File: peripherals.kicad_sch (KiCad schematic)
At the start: 61 parts, among them J801 Socket_Samtec_ERF5_2x20_ERF5-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, J802 JST_SH_1x4_SM04B-SRSS-TB-LF-SN, J803 JST_SH_1x4_SM04B-SRSS-TB-LF-SN, J804 JST_SH_1x2_SM02B-SRSS-TB-LF-SN, J805 JST_SH_1x6_SM06B-SRSS-TB-LF-SN, U801 PN7160A1_VFQFN, Y801 Resonator_27.12MHz_XRCGB

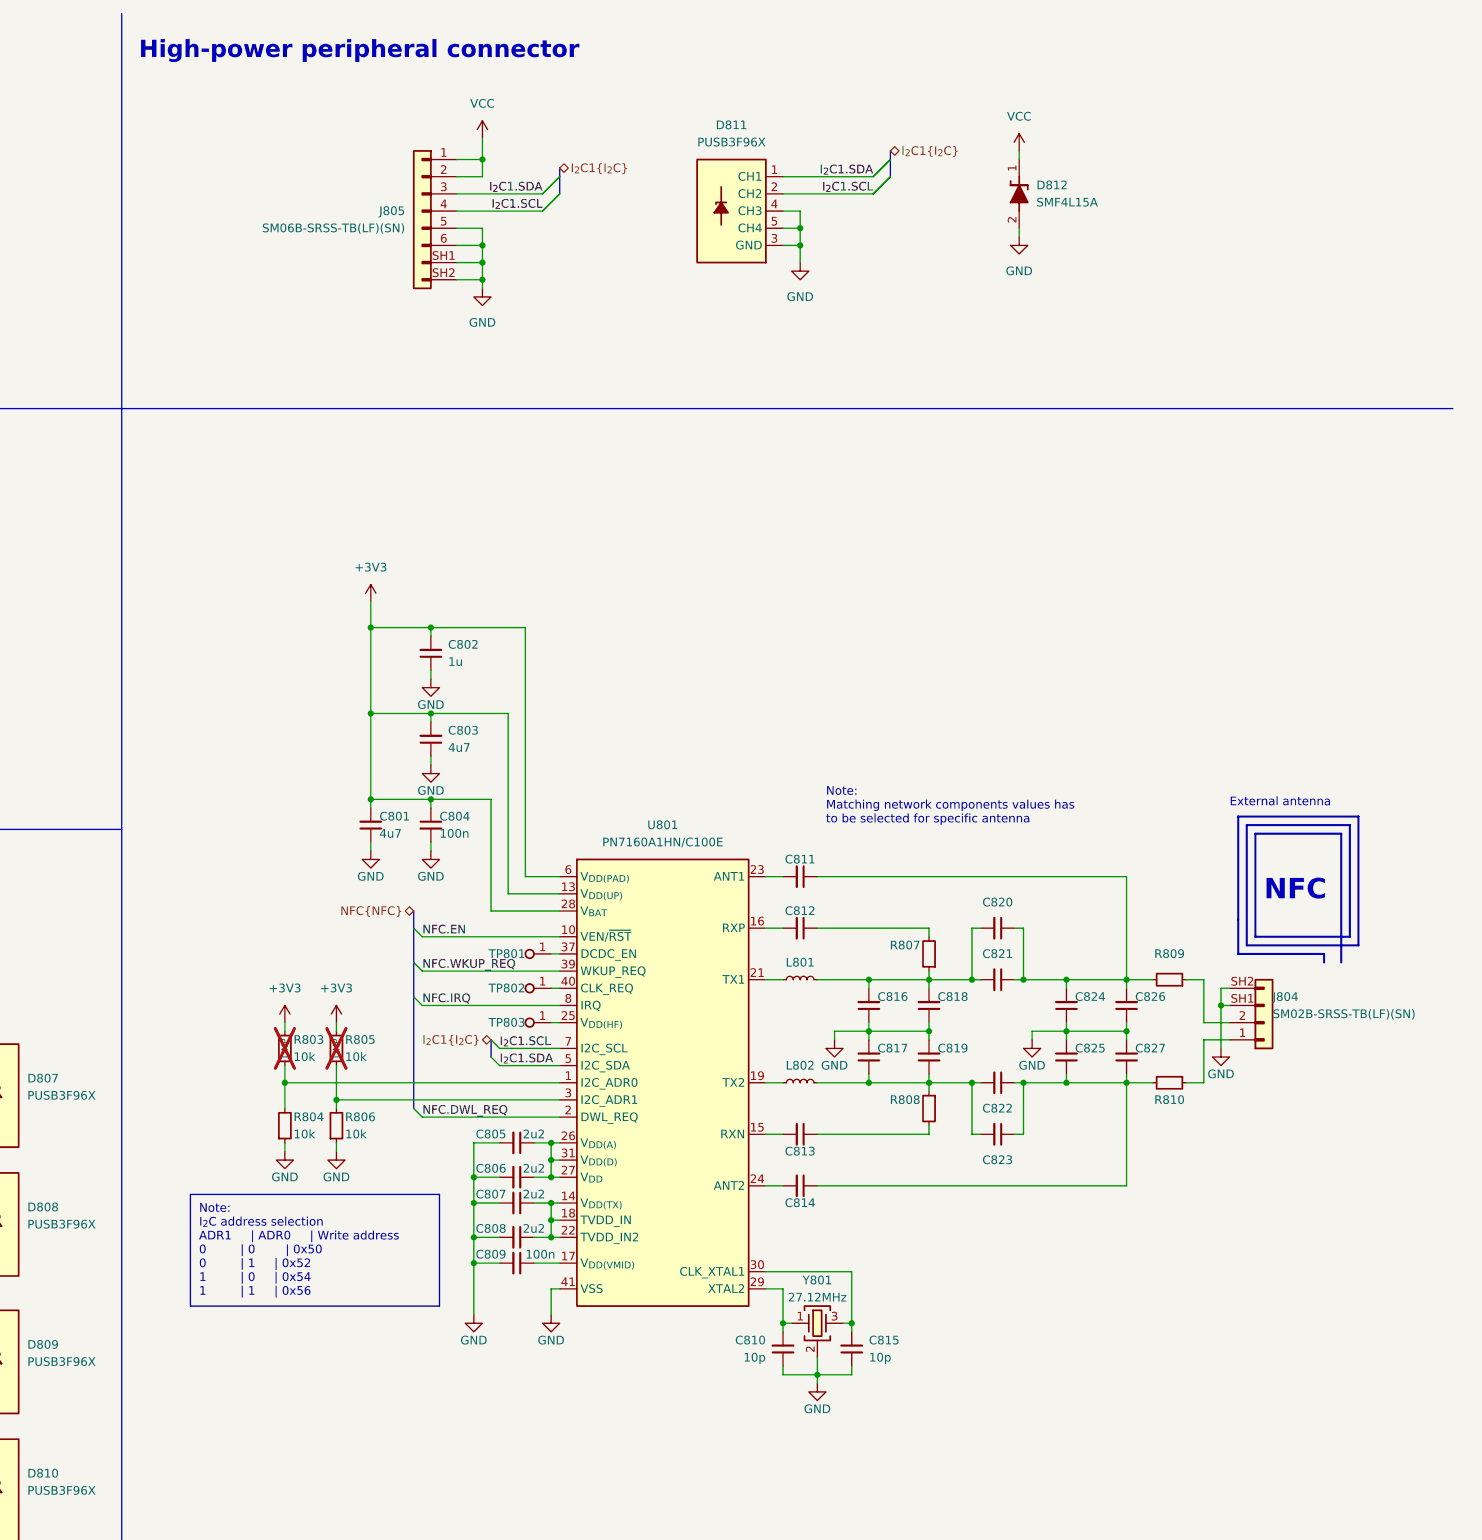
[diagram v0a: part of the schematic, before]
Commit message: Revert "[#58133] Add high-power peripheral connector"
This reverts commit a83347aca41b3b449620dbb955cb5f6a2460727a
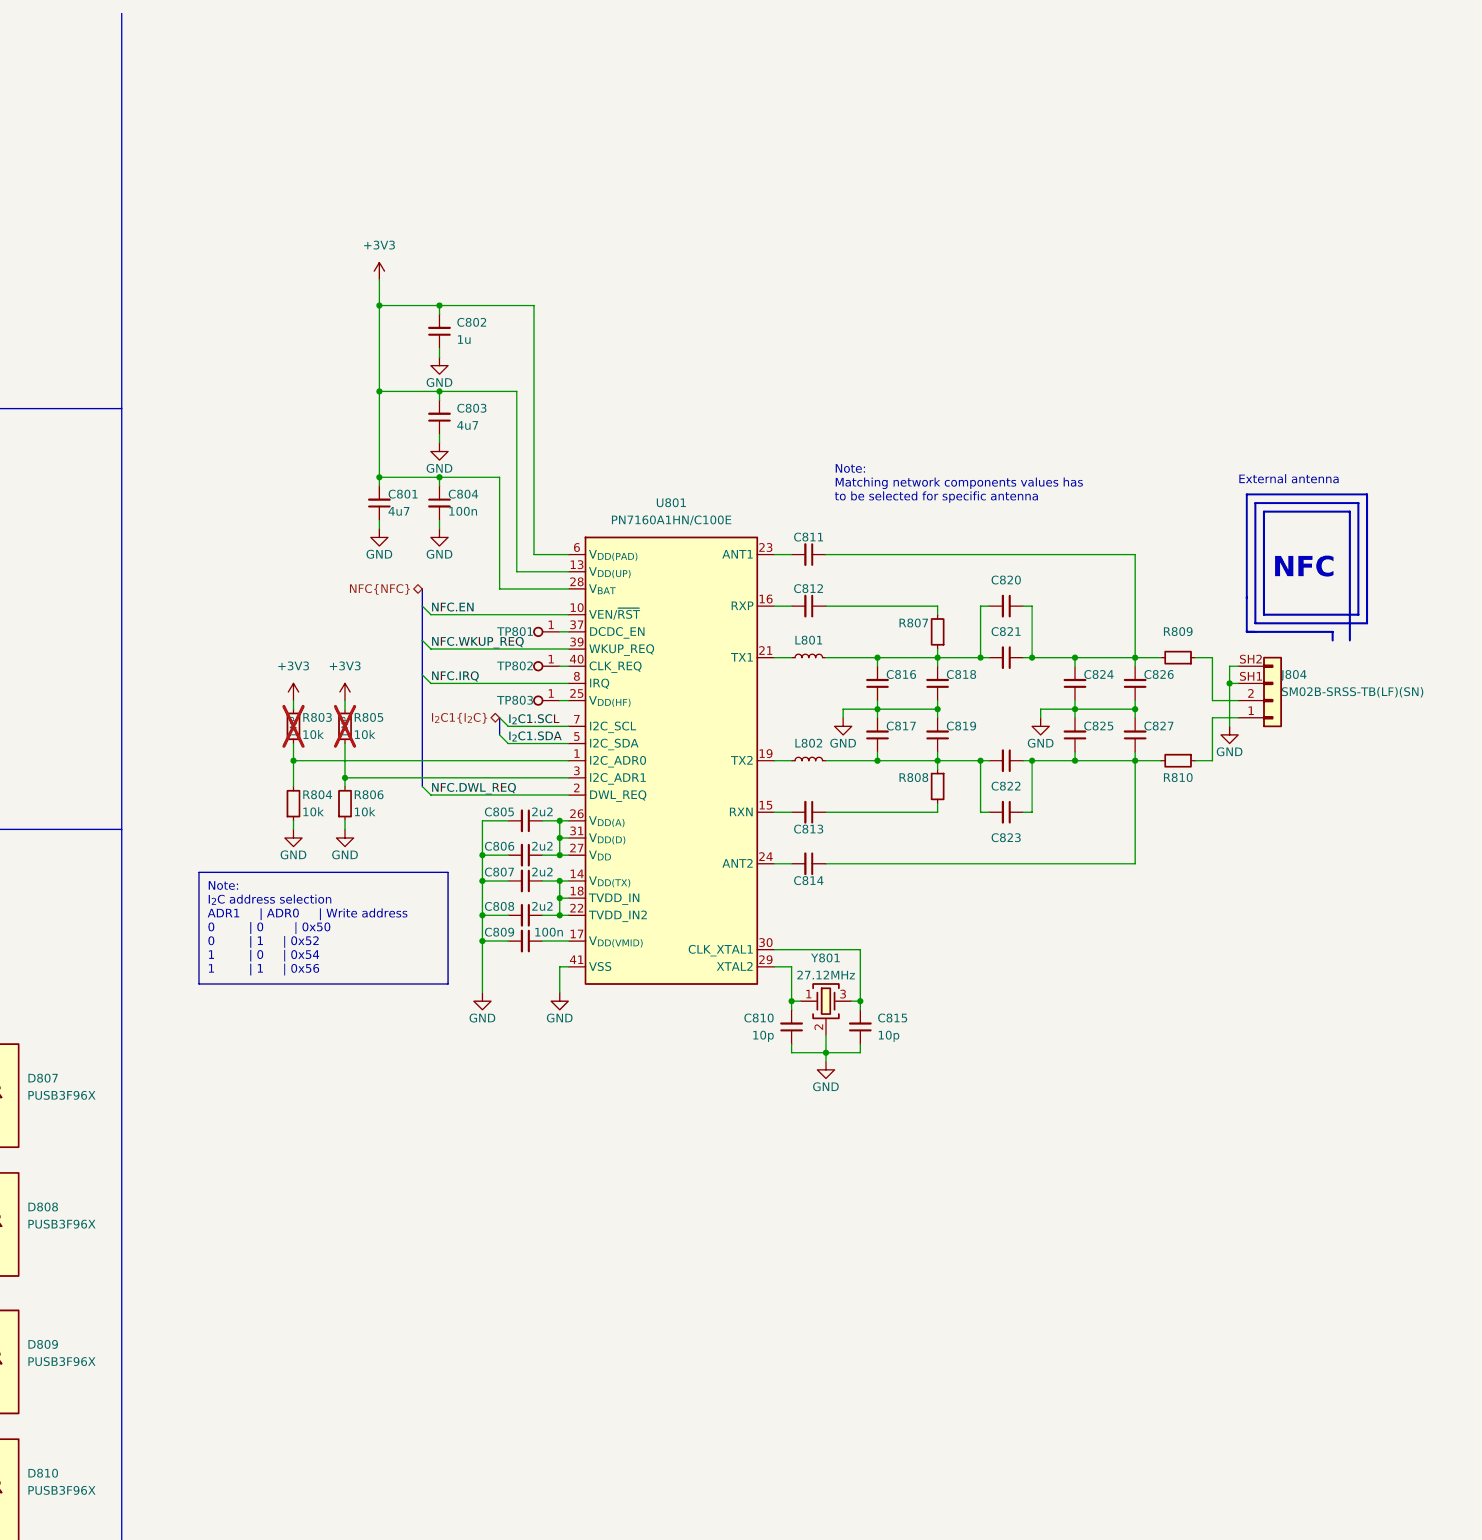
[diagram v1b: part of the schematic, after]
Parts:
- removed D811: PUSB3F96X_PASS, antmicro-footprints:Nexperia_DFN-10_2.5x1mm_P0.5mm, symbol antmicroTVSDiodes:PUSB3F96X_PASS
- removed D812: SMF4L15A, antmicro-footprints:SOD-123FL, symbol antmicroTVSDiodes:SMF4L15A
- removed J805: JST_SH_1x6_SM06B-SRSS-TB-LF-SN, antmicro-footprints:Conn_JST_SH_1x6_SM06B-SRSS-TB-LF-SN, symbol antmicroWire2BoardConnectors:JST_SH_1x6_SM06B-SRSS-TB-LF-SN
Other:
- note removed: "High-power peripheral connector"
- moved on the sheet: C801, C802, C803, C804, C805, C806, C807, C808, C809, C810, C811, C812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

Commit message: [#58133] Add high-power peripheral connector
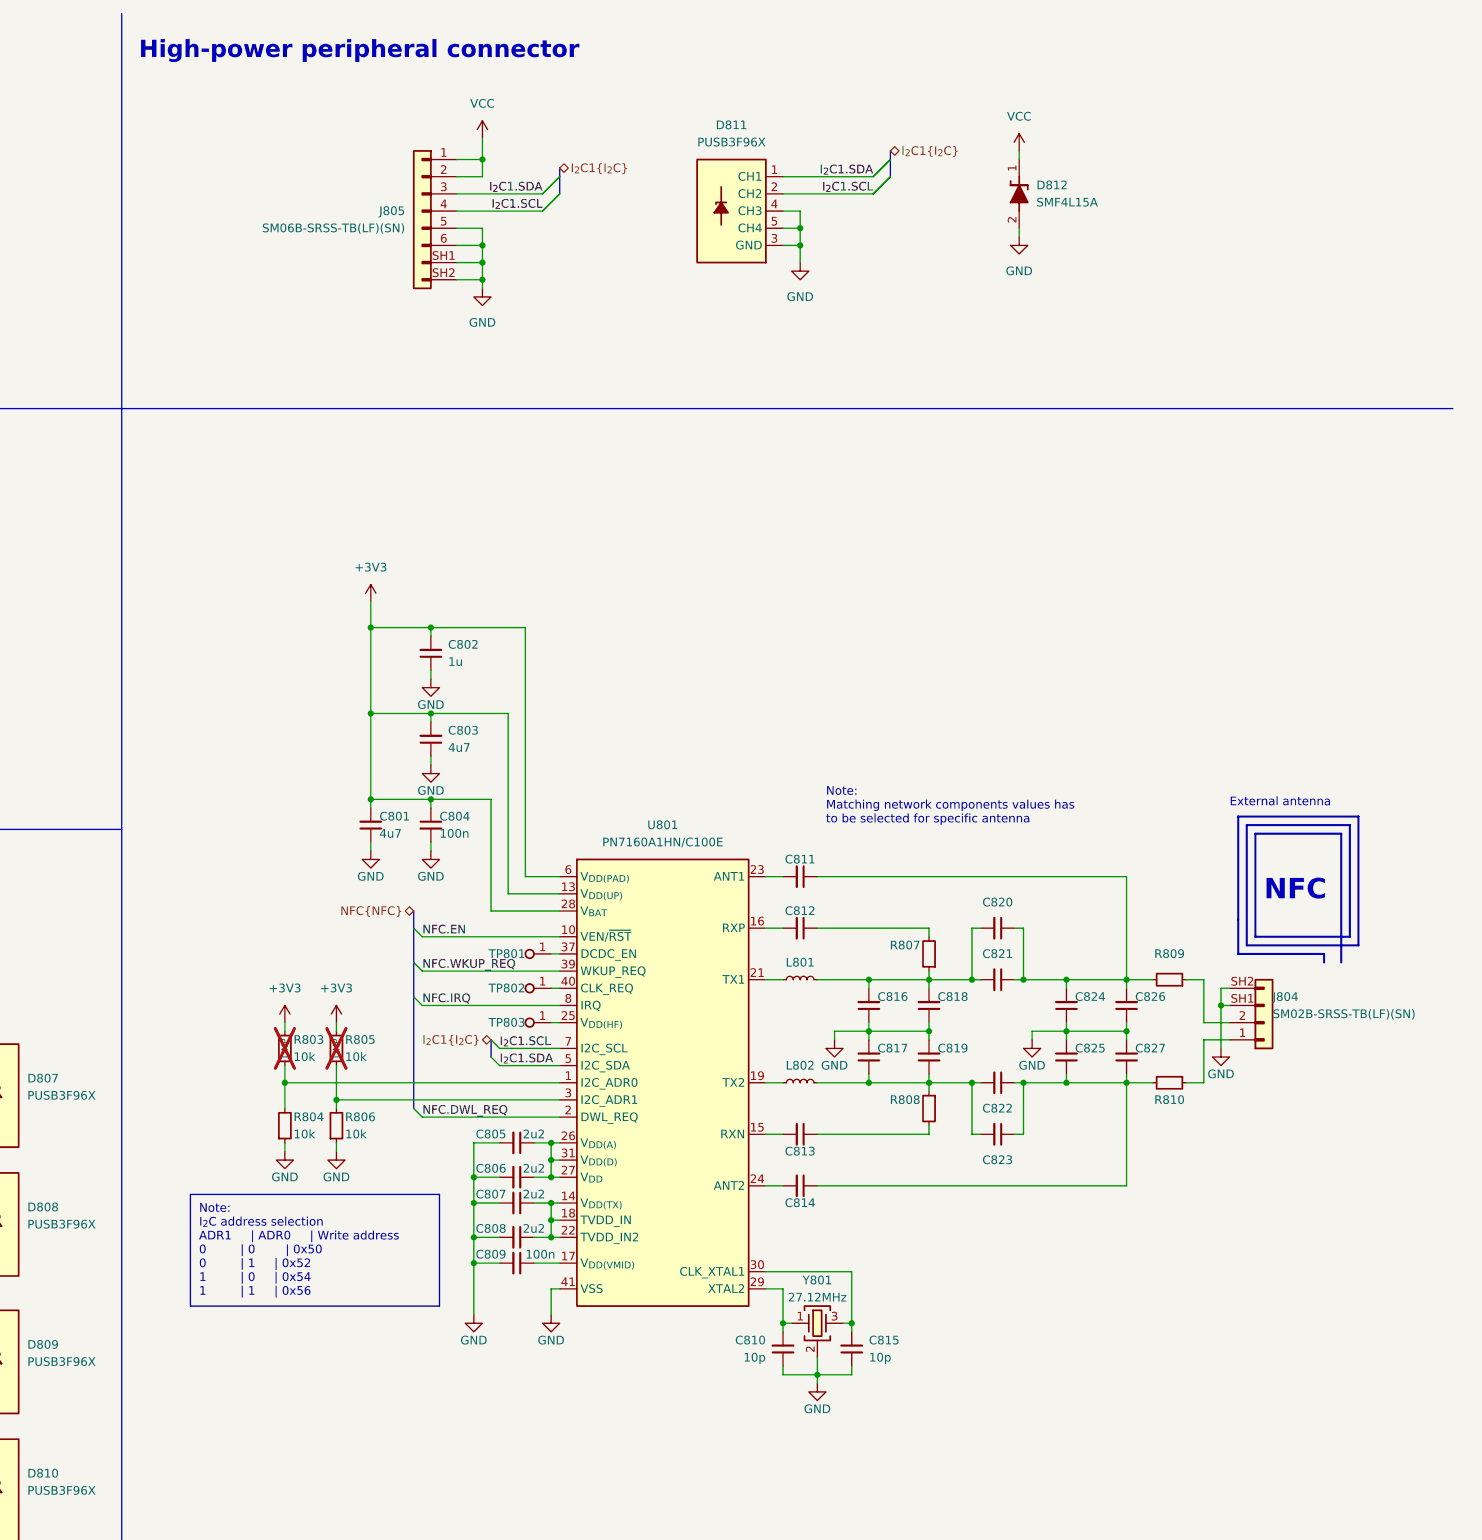
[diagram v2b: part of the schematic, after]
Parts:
- added D811: PUSB3F96X_PASS, antmicro-footprints:Nexperia_DFN-10_2.5x1mm_P0.5mm, symbol antmicroTVSDiodes:PUSB3F96X_PASS
- added D812: SMF4L15A, antmicro-footprints:SOD-123FL, symbol antmicroTVSDiodes:SMF4L15A
- added J805: JST_SH_1x6_SM06B-SRSS-TB-LF-SN, antmicro-footprints:Conn_JST_SH_1x6_SM06B-SRSS-TB-LF-SN, symbol antmicroWire2BoardConnectors:JST_SH_1x6_SM06B-SRSS-TB-LF-SN
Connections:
- net GND: now also D811.3 (GND), D811.4 (CH3), D811.5 (CH4), D811.6 (CH4), D811.7 (CH3), D811.8 (GND), D812.2, J805.5, J805.6, J805.SH1, J805.SH2
- net I_{2}C1.SCL: now also D811.2 (CH2), D811.9 (CH2), J805.4
- net I_{2}C1.SDA: now also D811.1 (CH1), D811.10 (CH1), J805.3
- new net VCC: D812.1, J805.1, J805.2
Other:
- note added: "High-power peripheral connector"
- moved on the sheet: C801, C802, C803, C804, C805, C806, C807, C808, C809, C810, C811, C812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
